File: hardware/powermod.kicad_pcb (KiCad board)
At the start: 4 copper layers, 65 x 40 mm, 77 parts, among them J1 USB_C_IN, J2 USB_C_OUT, J3 JST_PH_2, J4 STEMMA_QT, J5 SWD_HDR, Q1 AON7407, Q2 AON7407, Q3 BSS138, SW1 BUTTON, U1 BM8563, U2 PY32F003F18P6, U3 TPS63020DSJR, U4 TP4056, U5 XC6206P332MR, Y1 32.768kHz

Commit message: hardware: final routed board - 0 DRC, 0 unrouted, all fixes in
Full verification: DRC 0, unrouted 0, pad-diff 226/226. USB-C CC on A5/B5,
L1N/L2 uniform 1.1mm, U3 EP 4 tented GND ties, R14.2 tied. 447 tracks, 196 vias.

Co-Authored-By: Claude Opus 4.8 <noreply@anthropic.com>
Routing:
- net VOUT: track 47.6 -> 73.4 mm
- net VBUS: track 24.3 -> 42.7 mm
- net L1N: track 5.31 -> 9.64 mm
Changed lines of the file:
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@@
 	)
 	(segment
+		(start 8.945 12.55)
+		(end 9.785252 12.55)
+		(width 0.6)
+		(layer "F.Cu")
+		(net "VBUS")
+	)
+	(segment
 		(start 12.7849 17.8251)
 		(end 12.7728 17.8372)
@@
 	)
 	(segment
+		(start 10.17 12.934748)
+		(end 10.17 17.28)
+		(width 0.6)
+		(layer "F.Cu")
+		(net "VBUS")
+	)
+	(segment
 		(start 12.7607 17.8493)
 		(end 12.05 18.56)
@@
 	)
 	(segment
+		(start 14.268232 9.5)
+		(end 14.99 9.5)
+		(width 0.6)
+		(layer "F.Cu")
+		(net "VBUS")
+	)
+	(segment
+		(start 9.785252 12.55)
+		(end 10.17 12.934748)
+		(width 0.6)
+		(layer "F.Cu")
+		(net "VBUS")
+	)
+	(segment
 		(start 12.955 17.655)
 		(end 12.8578 17.7522)
@@
 	)
 	(segment
+		(start 11.218232 12.55)
+		(end 14.268232 9.5)
+		(width 0.6)
+		(layer "F.Cu")
+		(net "VBUS")
+	)
+	(segment
+		(start 8.945 17.45)
+		(end 12.75 17.45)
+		(width 0.6)
+		(layer "F.Cu")
+		(net "VBUS")
+	)
+	(segment
 		(start 14.99 9.7233)
 		(end 14.99 9.5)
@@
 	)
 	(segment
+		(start 10.17 17.28)
+		(end 10 17.45)
+		(width 0.6)
+		(layer "F.Cu")
+		(net "VBUS")
+	)
+	(segment
 		(start 15.0259 9.7592)
 		(end 14.99 9.7233)
@@
 	)
 	(segment
+		(start 8.945 12.55)
+		(end 11.218232 12.55)
+		(width 0.6)
+		(layer "F.Cu")
+		(net "VBUS")
+	)
+	(segment
 		(start 15.5033 22.2433)
 		(end 16 22.2433)
@@
 		(net "VBUS")
 	)
+	(segment
+		(start 10 17.45)
+		(end 8.945 17.45)
+		(width 0.6)
+		(layer "F.Cu")
+		(net "VBUS")
+	)
+	(segment
+		(start 12.75 17.45)
+		(end 12.955 17.655)
+		(width 0.6)
+		(layer "F.Cu")
+		(net "VBUS")
+	)
 	(via
 		(at 10 27.5)
@@
 	)
 	(segment
-		(start 37.9 10.695)
-		(end 38.55 10.695)
-		(width 0.3004)
-		(layer "F.Cu")
-		(net "VSYS")
-	)
-	(segment
 		(start 22.01 22.53)
 		(end 22.01 24)
@@
 	)
 	(segment
+		(start 38.204 10.999)
+		(end 38.05 10.845)
+		(width 0.6)
+		(layer "F.Cu")
+		(net "VSYS")
+	)
+	(segment
+		(start 38.05 10.845)
+		(end 38.05 10.695)
+		(width 0.6)
+		(layer "F.Cu")
+		(net "VSYS")
+	)
+	(segment
 		(start 18 24.35)
 		(end 18 25)
@@
 	)
 	(segment
+		(start 38.246 13.195)
+		(end 38.246 10.999)
+		(width 0.6)
+		(layer "F.Cu")
+		(net "VSYS")
+	)
+	(segment
 		(start 27.275 28)
 		(end 27.4375 27.8375)
@@
 	)
 	(segment
-		(start 38.246 10.999)
-		(end 38.55 10.695)
-		(width 0.3004)
-		(layer "F.Cu")
-		(net "VSYS")
-	)
-	(segment
 		(start 18 25)
 		(end 20.0779 27.0779)
@@
 	)
 	(segment
-		(start 38.246 10.999)
-		(end 38.246 13.195)
+		(start 20.0779 29.0139)
+		(end 19.7918 29.3)
 		(width 0.6)
 		(layer "F.Cu")
@@
 	)
 	(segment
-		(start 20.0779 29.0139)
-		(end 19.7918 29.3)
+		(start 27.275 28)
+		(end 26.2611 29.0139)
 		(width 0.6)
 		(layer "F.Cu")
@@
 	)
 	(segment
-		(start 27.275 28)
-		(end 26.2611 29.0139)
+		(start 38.246 10.999)
+		(end 38.204 10.999)
 		(width 0.6)
 		(layer "F.Cu")
@@
 	)
 	(segment
+		(start 38.246 10.999)
+		(end 38.55 10.695)
+		(width 0.6)
+		(layer "F.Cu")
+		(net "VSYS")
+	)
+	(segment
 		(start 18 28.9759)
 		(end 18 28.65)
@@
 	)
 	(segment
-		(start 38.55 7.795)
-		(end 38.2125 7.795)
-		(width 0.3004)
-		(layer "F.Cu")
-		(net "VOUT")
-	)
-	(segment
 		(start 49 27.0849)
 		(end 49 26.6798)
@@
 	)
 	(segment
+		(start 51.319999 27.49)
+		(end 51 27.49)
+		(width 0.6)
+		(layer "F.Cu")
+		(net "VOUT")
+	)
+	(segment
 		(start 35.6566 4.3016)
 		(end 35.6566 4.1799)
@@
 	)
 	(segment
+		(start 46.378629 27.49)
+		(end 49 27.49)
+		(width 0.6)
+		(layer "F.Cu")
+		(net "VOUT")
+	)
+	(segment
 		(start 35.0349 4.1799)
 		(end 35 4.145)
@@
 	)
 	(segment
+		(start 38.5 35.368629)
+		(end 46.378629 27.49)
+		(width 0.6)
+		(layer "F.Cu")
+		(net "VOUT")
+	)
+	(segment
+		(start 38.55 7.195)
+		(end 38.55 7.795)
+		(width 0.6)
+		(layer "F.Cu")
+		(net "VOUT")
+	)
+	(segment
+		(start 47.55 28.44)
+		(end 48.5 27.49)
+		(width 0.6)
+		(layer "F.Cu")
+		(net "VOUT")
+	)
+	(segment
 		(start 37.5 6.145)
 		(end 35.6566 4.3016)
@@
 	)
 	(segment
-		(start 38.2125 7.795)
-		(end 38.2125 6.205)
+		(start 37.5 6.145)
+		(end 38.0498 6.6948)
 		(width 0.6)
 		(layer "F.Cu")
@@
 	)
 	(segment
+		(start 38.5 37)
+		(end 38.5 35.368629)
+		(width 0.6)
+		(layer "F.Cu")
+		(net "VOUT")
+	)
+	(segment
 		(start 42.65 3.195)
 		(end 43.338 3.883)
@@
 	)
 	(segment
+		(start 52.45 28.620001)
+		(end 51.319999 27.49)
+		(width 0.6)
+		(layer "F.Cu")
+		(net "VOUT")
+	)
+	(segment
 		(start 49 27.1355)
 		(end 49 27.1228)
@@
 	)
 	(segment
+		(start 47.55 31.005)
+		(end 47.55 28.44)
+		(width 0.6)
+		(layer "F.Cu")
+		(net "VOUT")
+	)
+	(segment
 		(start 39 6.205)
 		(end 38.2125 6.205)
@@
 	)
 	(segment
+		(start 37.5 6.145)
+		(end 38.55 7.195)
+		(width 0.6)
+		(layer "F.Cu")
+		(net "VOUT")
+	)
+	(segment
 		(start 49 27.1194)
 		(end 49 27.1192)
@@
 	)
 	(segment
+		(start 52.45 31.005)
+		(end 52.45 28.620001)
+		(width 0.6)
+		(layer "F.Cu")
+		(net "VOUT")
+	)
+	(segment
+		(start 38.0498 6.6948)
+		(end 38.0498 7.795)
+		(width 0.6)
+		(layer "F.Cu")
+		(net "VOUT")
+	)
+	(segment
 		(start 49 27.49)
 		(end 49 27.2874)
@@
 	)
 	(segment
-		(start 38.2125 7.795)
-		(end 37.9 7.795)
-		(width 0.3004)
+		(start 48.5 27.49)
+		(end 49 27.49)
+		(width 0.6)
 		(layer "F.Cu")
 		(net "VOUT")
@@
 	)
 	(segment
-		(start 34.9517 6.345)
-		(end 36.0029 7.3962)
+		(start 33.85 7.695)
+		(end 36.9998 7.695)
 		(width 1.1)
 		(layer "F.Cu")
@@
 	(segment
 		(start 32.5 6.345)
-		(end 34.9517 6.345)
+		(end 33.85 7.695)
 		(width 1.1)
 		(layer "F.Cu")
@@
 	)
 	(segment
-		(start 36.2012 7.3962)
-		(end 36.6 7.795)
-		(width 0.3004)
-		(layer "F.Cu")
-		(net "L2")
-	)
-	(segment
-		(start 37.25 7.795)
-		(end 36.6 7.795)
-		(width 0.3004)
-		(layer "F.Cu")
-		(net "L2")
-	)
-	(segment
-		(start 36.0029 7.3962)
-		(end 36.2012 7.3962)
+		(start 32.5 12.045)
+		(end 35.35 12.045)
 		(width 1.1)
 		(layer "F.Cu")
-		(net "L2")
+		(net "L1N")
 	)
 	(segment
-		(start 35.25 12.045)
-		(end 36.6 10.695)
-		(width 0.3004)
+		(start 35.75 12.045)
+		(end 37 10.795)
+		(width 1.1)
 		(layer "F.Cu")
 		(net "L1N")
 	)
 	(segment
-		(start 32.5 12.045)
-		(end 35.25 12.045)
+		(start 35.35 12.045)
+		(end 36.6 10.795)
 		(width 1.1)
 		(layer "F.Cu")
@@
 	)
 	(segment
-		(start 36.6 10.695)
-		(end 37.25 10.695)
-		(width 0.3004)
+		(start 32.5 12.045)
+		(end 35.75 12.045)
+		(width 1.1)
 		(layer "F.Cu")
 		(net "L1N")

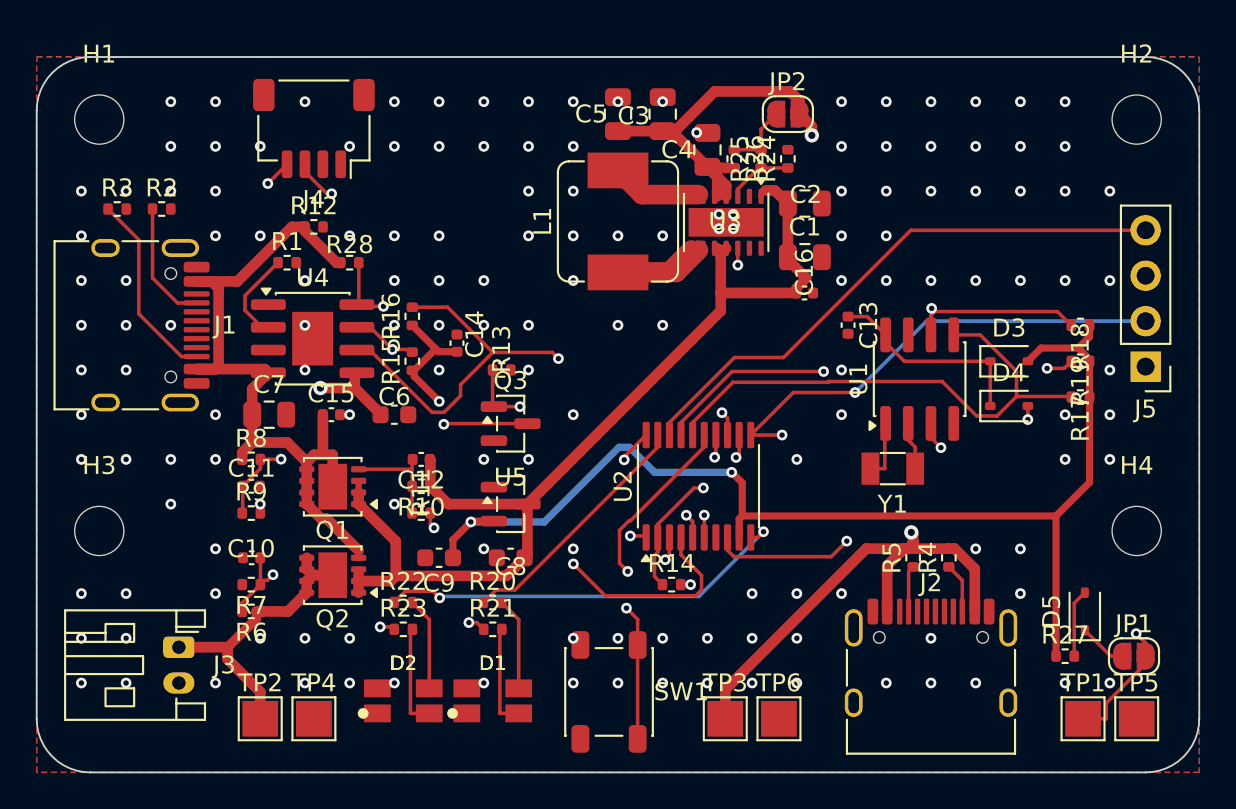
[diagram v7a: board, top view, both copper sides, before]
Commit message: hardware: reroute for flush connectors + carry CPL offset to new positions
User moved J1 (-0.9mm west) and J2 (+0.95mm south) to sit the USB-C openings
flush with the board edges. Full reroute with pre-placed EP(4)+R14.2 GND vias
(deterministic). pad-diff 226/226, CC on A5/B5, EP 4 ties, R14.2 tied, 0
shorts/clearance.

CPL: kept the tuned 1.36mm origin->pad offset, applied to the new origins ->
J1 Mid X 5.360, J2 Mid Y -34.640 (contacts stay centered on pads).

Remaining (user's usual finish): 4 track_width (L1N/L2 necks) + 6 unconnected
(the fine-pitch USB-C escapes).

Co-Authored-By: Claude Opus 4.8 <noreply@anthropic.com>
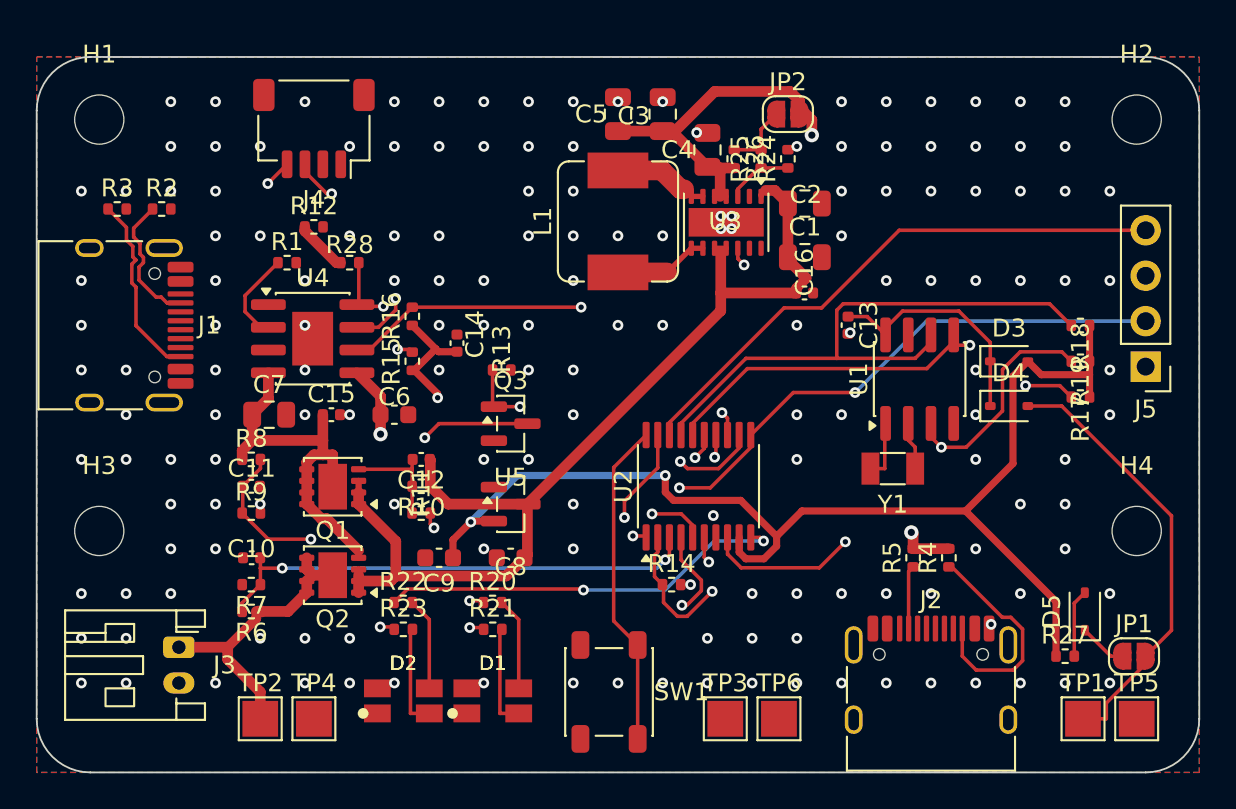
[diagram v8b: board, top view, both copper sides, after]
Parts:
- moved J2 0.95 mm to (50.0, 36.0)
- moved J1 0.90 mm to (4.00, 15.0)
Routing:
- net VOUT: track 73.4 -> 47.8 mm
- net VBUS: track 42.7 -> 24.7 mm
- net CC2_OUT: track 2.81 -> 12.8 mm
- net RTC_SCL: track 27.0 -> 33.4 mm, vias 2 -> 0
- net CONV_EN: track 22.6 -> 27.6 mm
- net RTC_SDA: track 29.8 -> 25.4 mm, vias 0 -> 2
- net L1N: track 9.64 -> 5.31 mm
- net LED_BAT_B: track 55.6 -> 51.7 mm
- net VBUS_DIV: track 34.8 -> 37.7 mm
- net LED_PWR_A: track 14.0 -> 16.8 mm, vias 0 -> 2
- net CHG_CHRG: track 27.3 -> 30.1 mm, vias 2 -> 3
- net BUTTON: track 20.8 -> 18.3 mm, vias 2 -> 0
- net RTC_INT: track 28.8 -> 31.2 mm, vias 3 -> 2
- net VBACKUP: track 22.4 -> 24.7 mm, vias 2 -> 0
- net VBAT: track 39.4 -> 37.3 mm
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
